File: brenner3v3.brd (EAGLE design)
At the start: 100 x 80 mm, 12 parts, among them IC1 REG1117, Q2 BC328, Q3 BC328

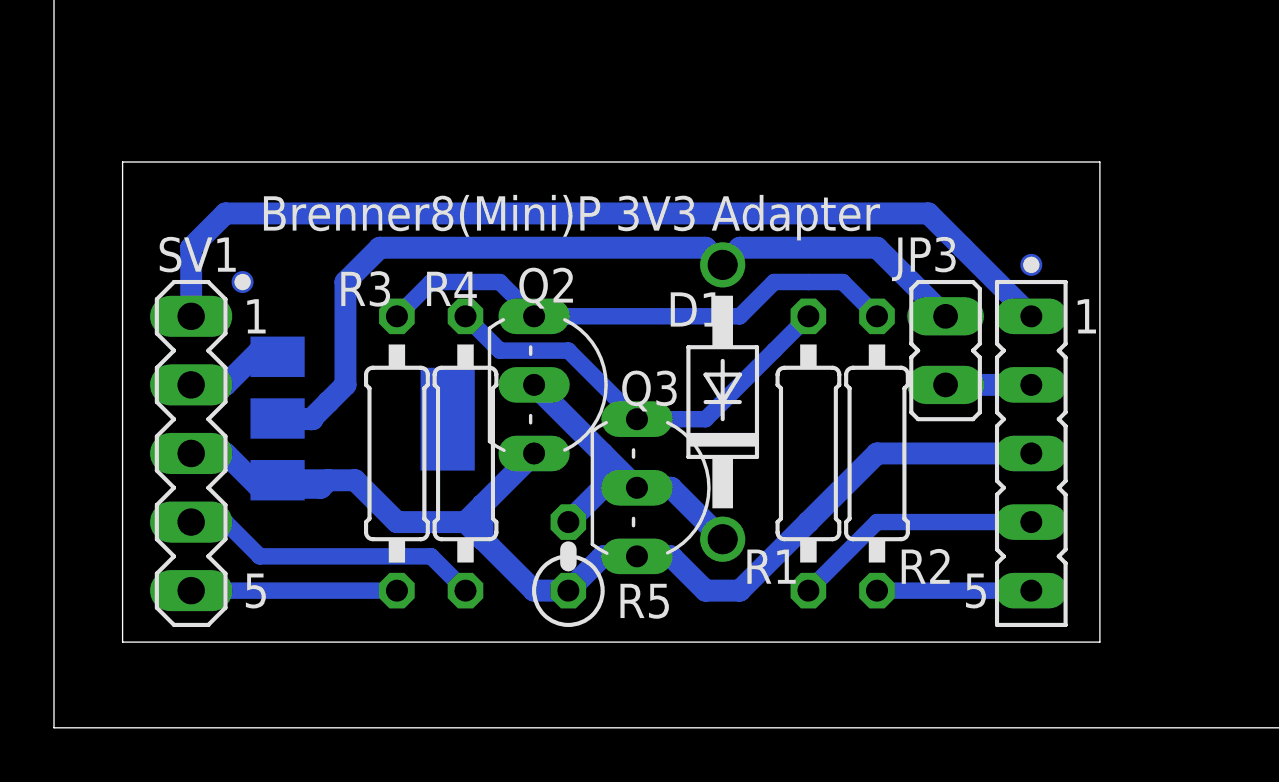
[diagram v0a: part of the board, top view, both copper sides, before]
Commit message: Metric drills
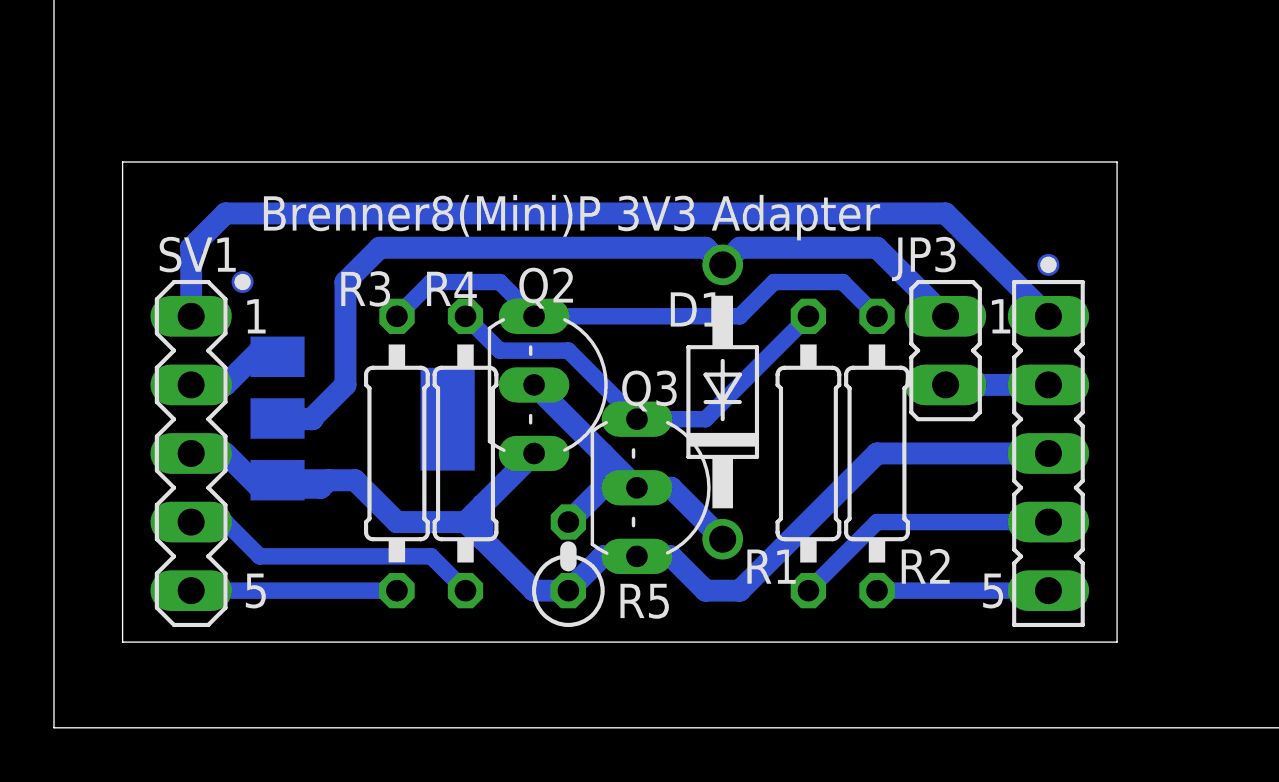
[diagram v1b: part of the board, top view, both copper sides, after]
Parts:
- moved SV2 0.63 mm to (36.8, 10.2)
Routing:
- net VSS: track 43.3 -> 44.0 mm
- net VPP: track 35.8 -> 36.4 mm
- net VDD3V3: track 3.17 -> 3.81 mm
- net N$9: track 5.71 -> 6.35 mm
- net N$8: track 9.31 -> 9.94 mm
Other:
- outline, holes or cut-outs redrawn
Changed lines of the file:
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@@
 <wire x1="100" y1="80" x2="0" y2="80" width="0" layer="20"/>
 <wire x1="0" y1="80" x2="0" y2="0" width="0" layer="20"/>
-<wire x1="2.54" y1="3.175" x2="38.735" y2="3.175" width="0" layer="20"/>
-<wire x1="38.735" y1="3.175" x2="38.735" y2="20.955" width="0" layer="20"/>
-<wire x1="38.735" y1="20.955" x2="2.54" y2="20.955" width="0" layer="20"/>
+<wire x1="2.54" y1="3.175" x2="39.37" y2="3.175" width="0" layer="20"/>
+<wire x1="39.37" y1="3.175" x2="39.37" y2="20.955" width="0" layer="20"/>
+<wire x1="39.37" y1="20.955" x2="2.54" y2="20.955" width="0" layer="20"/>
 <wire x1="2.54" y1="20.955" x2="2.54" y2="3.175" width="0" layer="20"/>
 <circle x="6.985" y="16.51" radius="0.4064" width="0" layer="16"/>
-<circle x="36.195" y="17.145" radius="0.4064" width="0" layer="16"/>
-<circle x="36.195" y="17.145" radius="0.3048" width="0" layer="21"/>
+<circle x="36.83" y="17.145" radius="0.4064" width="0" layer="16"/>
+<circle x="36.83" y="17.145" radius="0.3048" width="0" layer="21"/>
 <circle x="6.985" y="16.51" radius="0.3048" width="0" layer="21"/>
 <text x="6.985" y="14.605" size="1.27" layer="21">1</text>
-<text x="38.735" y="15.875" size="1.27" layer="21" rot="R180">1</text>
+<text x="35.56" y="15.875" size="1.27" layer="21" rot="R180">1</text>
 <text x="6.985" y="4.445" size="1.27" layer="21">5</text>
-<text x="33.655" y="4.445" size="1.27" layer="21">5</text>
+<text x="34.29" y="4.445" size="1.27" layer="21">5</text>
 <text x="7.62" y="18.415" size="1.27" layer="21">Brenner8(Mini)P 3V3 Adapter</text>
 </plain>
@@
 <attribute name="VALUE" x="2.159" y="12.7" size="1.27" layer="27" ratio="10" rot="R270"/>
 </element>
-<element name="SV2" library="con-lsta" package="FE05-1" value="" x="36.195" y="10.16" smashed="yes" rot="R270">
-<attribute name="OC_NEWARK" value="unknown" x="6.985" y="-11.43" size="1.778" layer="27" rot="R270" display="off"/>
-<attribute name="MPN" value="" x="6.985" y="-11.43" size="1.778" layer="27" rot="R270" display="off"/>
-<attribute name="MF" value="" x="6.985" y="-11.43" size="1.778" layer="27" rot="R270" display="off"/>
-<attribute name="OC_FARNELL" value="unknown" x="6.985" y="-11.43" size="1.778" layer="27" rot="R270" display="off"/>
-<attribute name="NAME" x="34.925" y="17.526" size="1.27" layer="25" ratio="10" display="off"/>
-<attribute name="VALUE" x="37.846" y="10.16" size="1.27" layer="27" ratio="10" rot="R270"/>
+<element name="SV2" library="con-lsta" package="FE05-1" value="" x="36.83" y="10.16" smashed="yes" rot="R270">
+<attribute name="OC_NEWARK" value="unknown" x="7.62" y="-11.43" size="1.778" layer="27" rot="R270" display="off"/>
+<attribute name="MPN" value="" x="7.62" y="-11.43" size="1.778" layer="27" rot="R270" display="off"/>
+<attribute name="MF" value="" x="7.62" y="-11.43" size="1.778" layer="27" rot="R270" display="off"/>
+<attribute name="OC_FARNELL" value="unknown" x="7.62" y="-11.43" size="1.778" layer="27" rot="R270" display="off"/>
+<attribute name="NAME" x="35.56" y="17.526" size="1.27" layer="25" ratio="10" display="off"/>
+<attribute name="VALUE" x="38.481" y="10.16" size="1.27" layer="27" ratio="10" rot="R270"/>
 </element>
 </elements>
@@
 <wire x1="22.86" y1="6.35" x2="24.13" y2="5.08" width="0.8128" layer="16"/>
 <wire x1="24.13" y1="5.08" x2="25.4" y2="5.08" width="0.8128" layer="16"/>
-<wire x1="25.4" y1="5.08" x2="27.94" y2="7.62" width="0.8128" layer="16"/>
-<wire x1="27.94" y1="7.62" x2="30.48" y2="10.16" width="0.8128" layer="16"/>
-<wire x1="30.48" y1="10.16" x2="36.195" y2="10.16" width="0.8128" layer="16"/>
+<wire x1="25.4" y1="5.08" x2="30.48" y2="10.16" width="0.8128" layer="16"/>
+<wire x1="30.48" y1="10.16" x2="36.83" y2="10.16" width="0.8128" layer="16"/>
 <wire x1="15.875" y1="8.255" x2="15.875" y2="6.985" width="0.8128" layer="16"/>
 </signal>
@@
 <wire x1="16.51" y1="13.97" x2="19.05" y2="13.97" width="0.6096" layer="16"/>
 <wire x1="19.05" y1="13.97" x2="21.59" y2="11.43" width="0.6096" layer="16"/>
-<wire x1="27.94" y1="15.24" x2="26.67" y2="13.97" width="0.6096" layer="16"/>
-<wire x1="26.67" y1="13.97" x2="24.13" y2="11.43" width="0.6096" layer="16"/>
+<wire x1="27.94" y1="15.24" x2="24.13" y2="11.43" width="0.6096" layer="16"/>
 <wire x1="24.13" y1="11.43" x2="21.59" y2="11.43" width="0.6096" layer="16"/>
 </signal>
@@
 <wire x1="16.51" y1="16.51" x2="17.78" y2="15.24" width="0.6096" layer="16"/>
 <wire x1="30.48" y1="15.24" x2="29.21" y2="16.51" width="0.6096" layer="16"/>
-<wire x1="29.21" y1="16.51" x2="27.94" y2="16.51" width="0.6096" layer="16"/>
-<wire x1="27.94" y1="16.51" x2="26.67" y2="16.51" width="0.6096" layer="16"/>
+<wire x1="29.21" y1="16.51" x2="26.67" y2="16.51" width="0.6096" layer="16"/>
 <wire x1="26.67" y1="16.51" x2="25.4" y2="15.24" width="0.6096" layer="16"/>
-<wire x1="25.4" y1="15.24" x2="19.05" y2="15.24" width="0.6096" layer="16"/>
-<wire x1="19.05" y1="15.24" x2="17.78" y2="15.24" width="0.6096" layer="16"/>
+<wire x1="25.4" y1="15.24" x2="17.78" y2="15.24" width="0.6096" layer="16"/>
 </signal>
 <signal name="N$8">
@@
 <contactref element="SV2" pad="4"/>
 <wire x1="27.94" y1="5.08" x2="30.48" y2="7.62" width="0.6096" layer="16"/>
-<wire x1="30.48" y1="7.62" x2="36.195" y2="7.62" width="0.6096" layer="16"/>
+<wire x1="30.48" y1="7.62" x2="36.83" y2="7.62" width="0.6096" layer="16"/>
 </signal>
 <signal name="N$9">
 <contactref element="R2" pad="2"/>
 <contactref element="SV2" pad="5"/>
-<wire x1="30.48" y1="5.08" x2="36.195" y2="5.08" width="0.6096" layer="16"/>
+<wire x1="30.48" y1="5.08" x2="36.83" y2="5.08" width="0.6096" layer="16"/>
 </signal>
 <signal name="VPP">
 <contactref element="SV1" pad="1"/>
 <contactref element="SV2" pad="1"/>
-<wire x1="36.195" y1="15.24" x2="33.655" y2="17.78" width="0.8128" layer="16"/>
-<wire x1="33.655" y1="17.78" x2="32.385" y2="19.05" width="0.8128" layer="16"/>
-<wire x1="32.385" y1="19.05" x2="6.35" y2="19.05" width="0.8128" layer="16"/>
+<wire x1="36.83" y1="15.24" x2="33.02" y2="19.05" width="0.8128" layer="16"/>
+<wire x1="33.02" y1="19.05" x2="6.35" y2="19.05" width="0.8128" layer="16"/>
 <wire x1="6.35" y1="19.05" x2="5.08" y2="17.78" width="0.8128" layer="16"/>
 <wire x1="5.08" y1="17.78" x2="5.08" y2="15.24" width="0.8128" layer="16"/>
@@
 <wire x1="9.525" y1="11.43" x2="9.5758" y2="11.43" width="0.8128" layer="16"/>
 <wire x1="9.5758" y1="11.43" x2="8.2804" y2="11.4554" width="0.8128" layer="16"/>
-<wire x1="9.525" y1="11.43" x2="10.16" y2="12.065" width="0.8128" layer="16"/>
-<wire x1="10.16" y1="12.065" x2="10.795" y2="12.7" width="0.8128" layer="16"/>
+<wire x1="9.525" y1="11.43" x2="10.795" y2="12.7" width="0.8128" layer="16"/>
 <wire x1="10.795" y1="12.7" x2="10.795" y2="16.51" width="0.8128" layer="16"/>
 <wire x1="10.795" y1="16.51" x2="12.065" y2="17.78" width="0.8128" layer="16"/>
@@
 <contactref element="JP3" pad="2"/>
 <contactref element="SV2" pad="2"/>
-<wire x1="33.02" y1="12.7" x2="36.195" y2="12.7" width="0.8128" layer="16"/>
+<wire x1="33.02" y1="12.7" x2="36.83" y2="12.7" width="0.8128" layer="16"/>
 </signal>
 </signals>

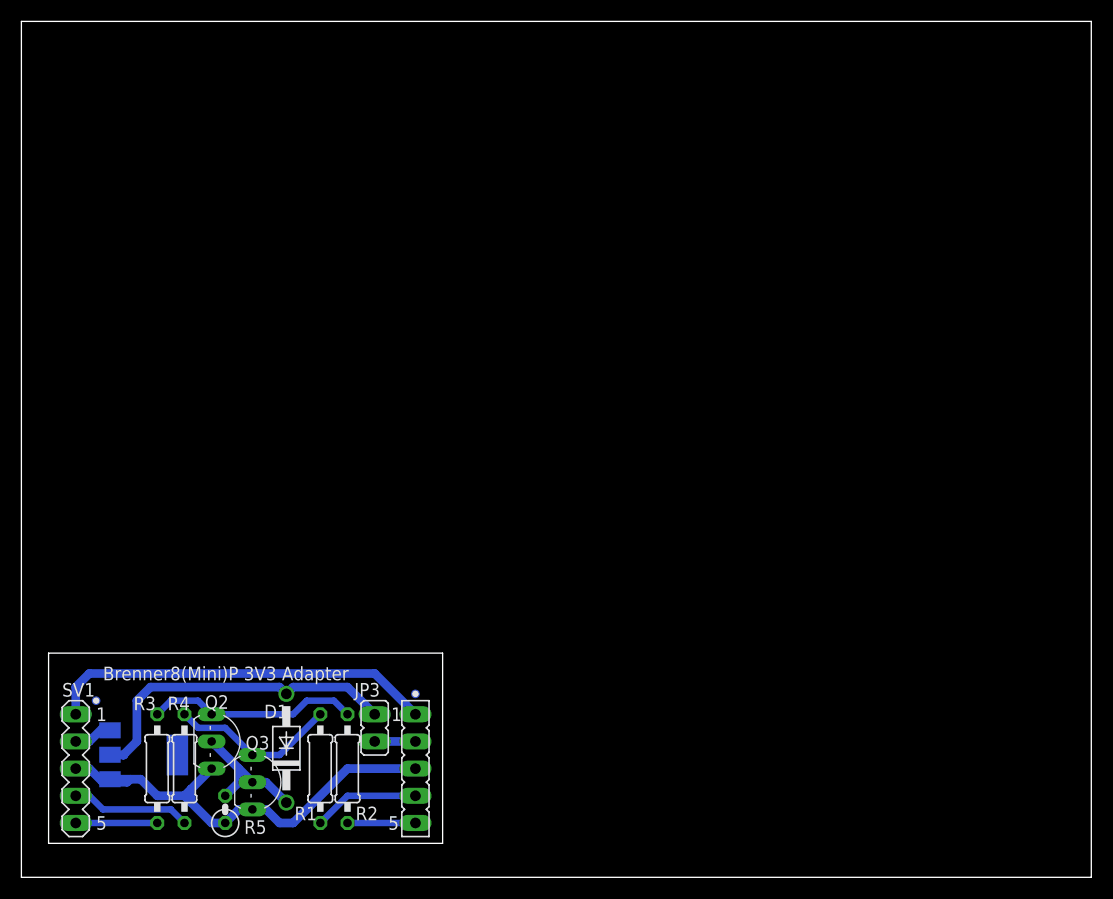
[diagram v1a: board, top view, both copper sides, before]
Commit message: Removed outer dimensions
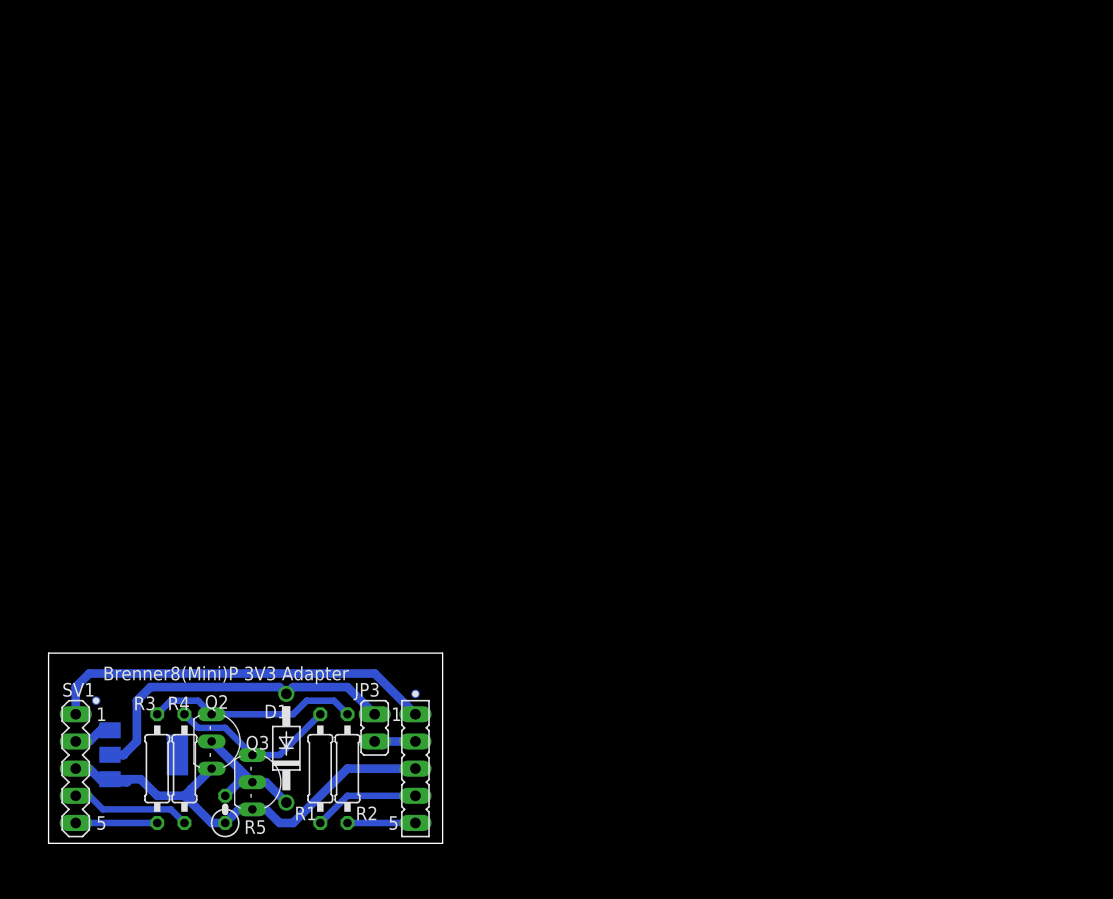
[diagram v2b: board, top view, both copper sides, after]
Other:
- board size 100 x 80 mm -> 36.8 x 17.8 mm
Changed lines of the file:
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@@
 <board>
 <plain>
-<wire x1="0" y1="0" x2="100" y2="0" width="0" layer="20"/>
-<wire x1="100" y1="0" x2="100" y2="80" width="0" layer="20"/>
-<wire x1="100" y1="80" x2="0" y2="80" width="0" layer="20"/>
-<wire x1="0" y1="80" x2="0" y2="0" width="0" layer="20"/>
 <wire x1="2.54" y1="3.175" x2="39.37" y2="3.175" width="0" layer="20"/>
 <wire x1="39.37" y1="3.175" x2="39.37" y2="20.955" width="0" layer="20"/>
